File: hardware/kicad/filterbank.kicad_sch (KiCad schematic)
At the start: 76 parts, among them J3 SMA/EDGE(RTL-SDR), U11 PE42582A(QFN24), U8 PE42582A(QFN24)

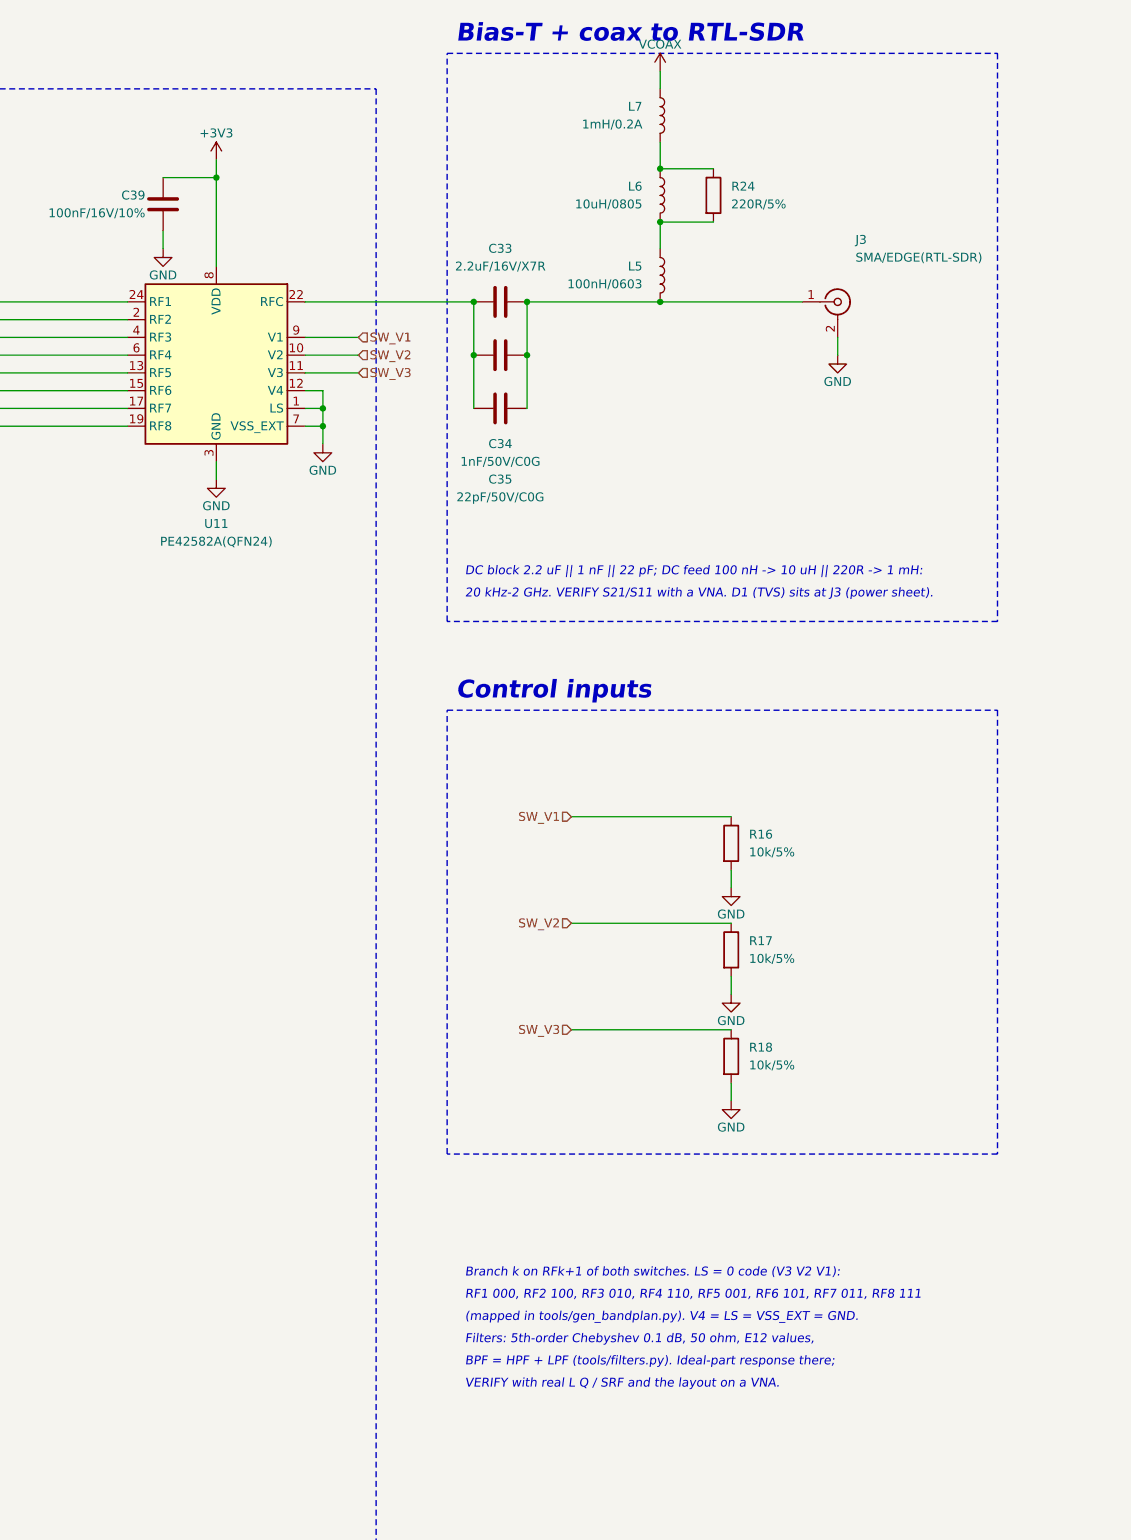
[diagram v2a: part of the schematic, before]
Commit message: U11 with LS = 1: mirror-port pairing makes the filter bank planar
PE42582 truth table: LS = 1 selects port 9 - port(LS = 0) for the same
V code, so U8 RF(k+1) pairs with U11 RF(8-k) and the 8 branches run
between the two facing switches on F.Cu without crossings. Same V lines,
firmware unchanged; at reset (V = 000) U8 RF1 / U11 RF8 = F0 THRU.
Symbol variant PE42582R (ports listed RF8..RF1, LS on top).

Co-Authored-By: Claude Opus 5.5 <noreply@anthropic.com>
Claude-Session: https://claude.ai/code/session_01YRUiF8Vp4242sya9Xyg3TV
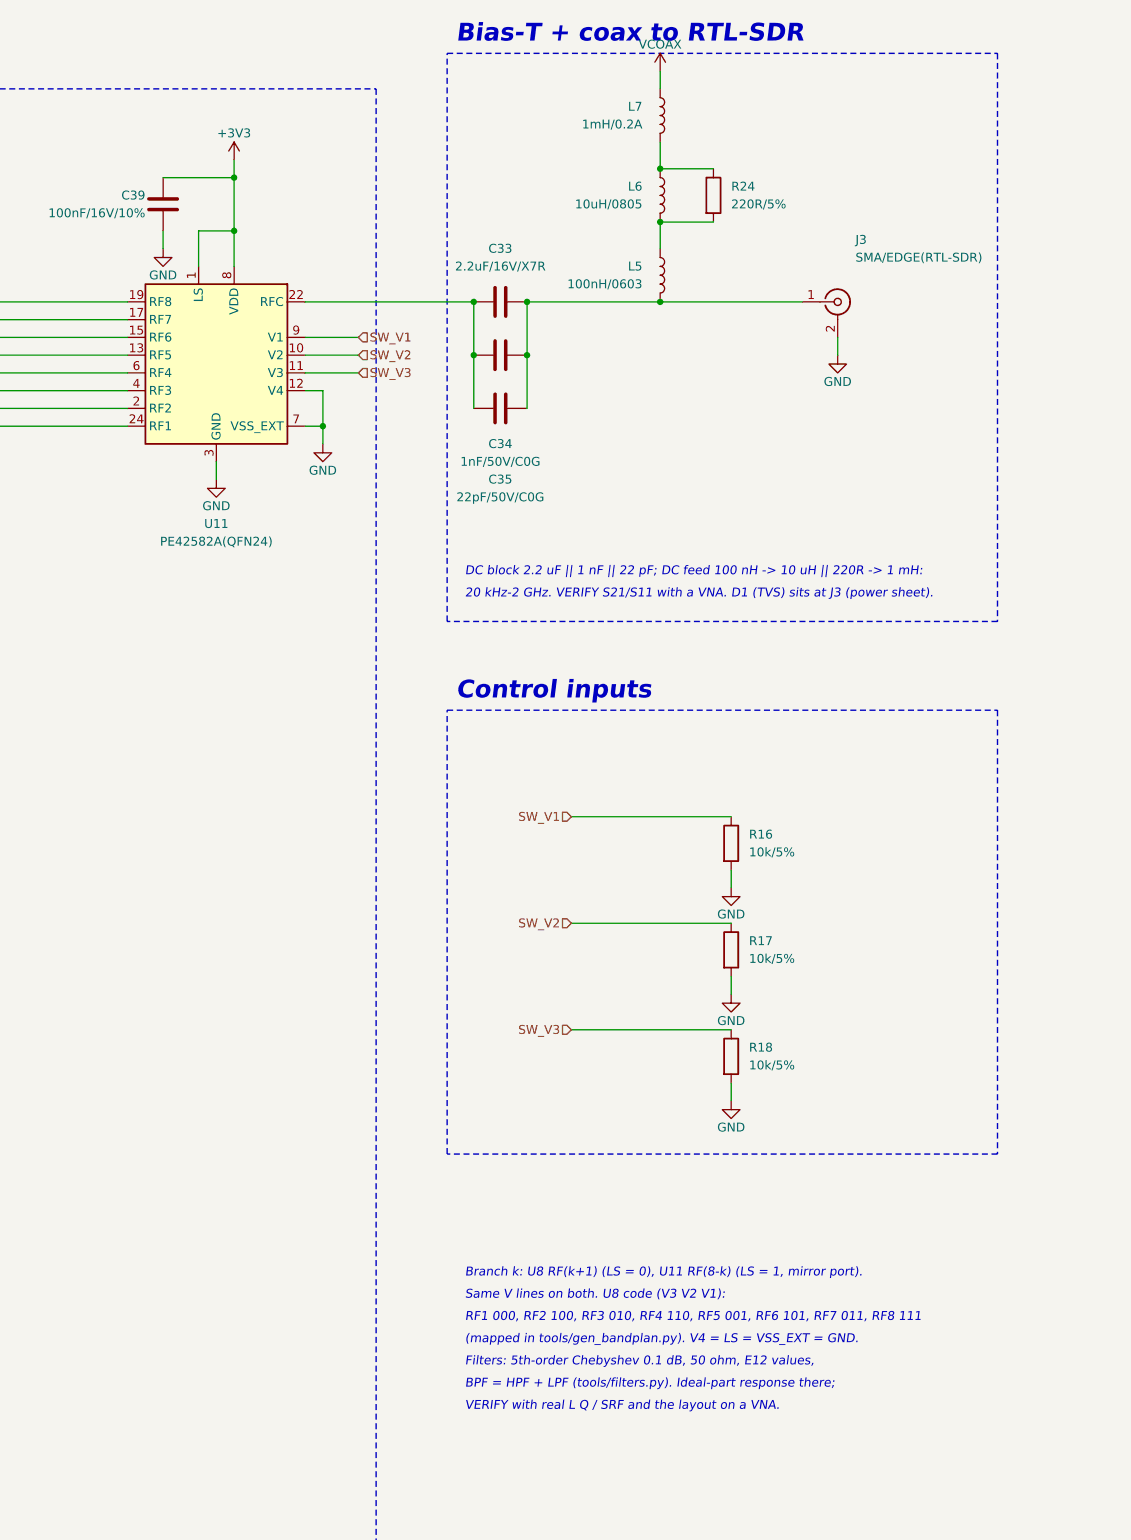
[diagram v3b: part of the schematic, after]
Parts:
- removed U11: PE42582A(QFN24), Package_DFN_QFN:QFN-24-1EP_4x4mm_P0.5mm_EP2.6x2.6mm, symbol coaxolotl:PE42582
- added U11: PE42582A(QFN24), Package_DFN_QFN:QFN-24-1EP_4x4mm_P0.5mm_EP2.6x2.6mm, symbol coaxolotl:PE42582R
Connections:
- net +3V3: now also U11.1 (LS), U11.8 (VDD)
- net GND: now also U11.12 (V4), U11.14 (GND), U11.16 (GND), U11.18 (GND), U11.20 (GND), U11.21 (GND), U11.23 (GND), U11.25 (GND), U11.3 (GND), U11.5 (GND), U11.7 (VSS_EXT)
- net SW_V1: now also U11.9 (V1)
- net SW_V2: now also U11.10 (V2)
- net SW_V3: now also U11.11 (V3)
- net at C406.1, L404.2: now also U11.6 (RF4)
- net at C103.1, L102.2: now also U11.17 (RF7)
- net at C33.1, C34.1, C35.1: now also U11.22 (RFC)
- net at C606.1, L604.2: now also U11.2 (RF2)
- net at C506.1, L504.2: now also U11.4 (RF3)
- net at C206.1, L204.2: now also U11.15 (RF6)
- net at C703.2: now also U11.24 (RF1)
- net at R21.2: now also U11.19 (RF8)
- net at C306.1, L304.2: now also U11.13 (RF5)
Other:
- note added: "Branch k: U8 RF(k+1) (LS = 0), U11 RF(8-k) (LS = 1, mirror port)."
- note added: "Same V lines on both. U8 code (V3 V2 V1):"
- note removed: "Branch k on RFk+1 of both switches. LS = 0 code (V3 V2 V1):"

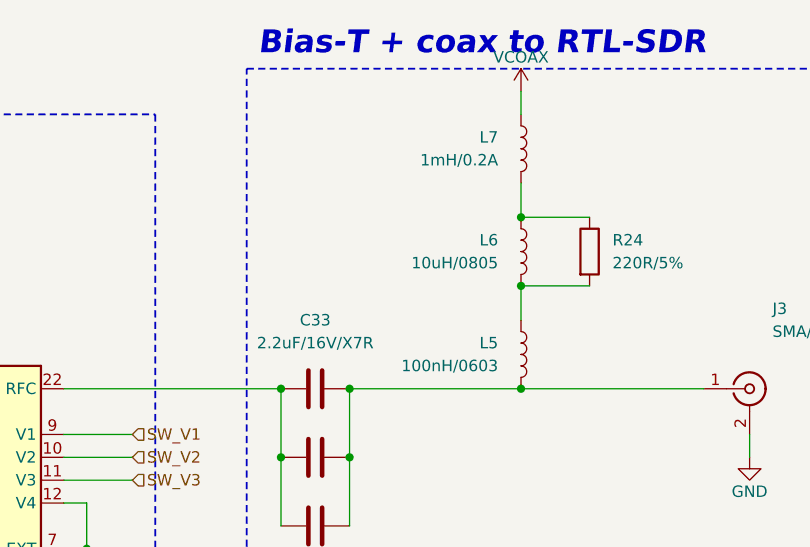
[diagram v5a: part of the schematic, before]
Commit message: L6: 10 uH 1210 wire-wound, 450 mA (LQH32CN100K33L, C86069) - it carries the whole coax DC
Co-Authored-By: Claude Opus 5.5 <noreply@anthropic.com>
Claude-Session: https://claude.ai/code/session_01YRUiF8Vp4242sya9Xyg3TV
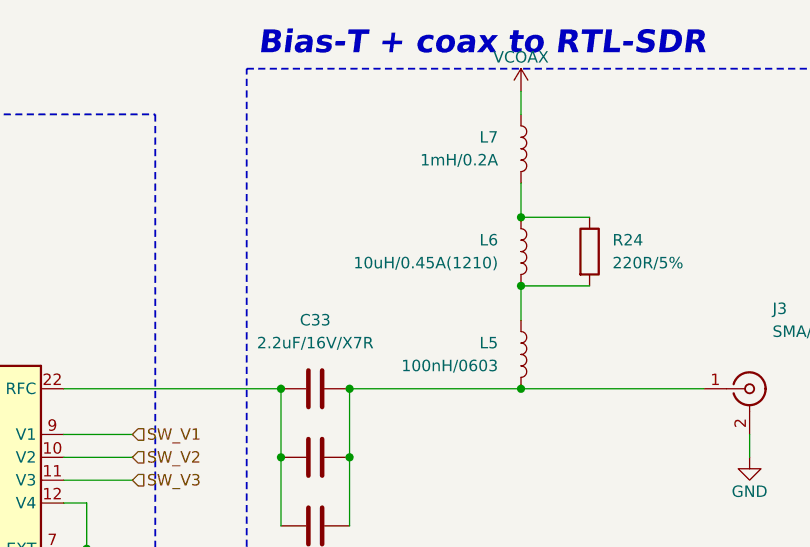
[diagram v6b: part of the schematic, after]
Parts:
- L6: value 10uH/0805 -> 10uH/0.45A(1210); footprint Inductor_SMD:L_0805_2012Metric -> Inductor_SMD:L_1210_3225Metric; MPN (none) -> LQH32CN100K33L

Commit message: Filter bank F7 retuned for the pad capacitance; LCSC codes for every fitted part; C10/J1/TP1/TP6 DNP
F7 (70/23cm HPF): C701/C703 12 pF, C702 6.8 pF, L701/L702 10 nH (was 8.2p/4.7p/15n), from the
openEMS lane N-port co-simulation (simu/f7_retune.py). filters.LAYOUT_TUNED carries the values.
L403/L404: Murata LQW18ANR33G00D C162651 (ceramic core) replaces LQW18CAR33J00D.
New codes, checked on JLC/LCSC (EasyEDA API) 2026-10-28: 12pF C38523, 6.8pF C1679, 10nH C15666,
820pF C701305, 1.5uH C317997, 2.2uH C41651, 4.7uH C139136.
Schematic sheets patched in place (build.py writes random uuids; the routed board links to the
current ones); build.py carries the same changes.

Co-Authored-By: Claude Opus 5.5 <noreply@anthropic.com>
Claude-Session: https://claude.ai/code/session_01YRUiF8Vp4242sya9Xyg3TV
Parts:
- C701, C703: value 8.2pF/50V/C0G -> 12pF/50V/C0G
- C702: value 4.7pF/50V/C0G -> 6.8pF/50V/C0G
- L701, L702: value 15nH/5% -> 10nH/5%
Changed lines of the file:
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@@
       )
     )
-    (property "Value" "8.2pF/50V/C0G"
+    (property "Value" "12pF/50V/C0G"
       (at 83.82 234.95 90)
       (effects
@@
       )
     )
-    (property "Value" "15nH/5%"
+    (property "Value" "10nH/5%"
       (at 101.6 245.11 0)
       (effects
@@
       )
     )
-    (property "Value" "4.7pF/50V/C0G"
+    (property "Value" "6.8pF/50V/C0G"
       (at 114.3 234.95 90)
       (effects
@@
       )
     )
-    (property "Value" "15nH/5%"
+    (property "Value" "10nH/5%"
       (at 132.08 245.11 0)
       (effects
@@
       )
     )
-    (property "Value" "8.2pF/50V/C0G"
+    (property "Value" "12pF/50V/C0G"
       (at 144.78 234.95 90)
       (effects

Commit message: MCU to EFM8BB21F16G-C-QFN20 (QSOP24 end of life), BWSMA-KE-P001 edge SMA, Brightking GDT
U5: QFN20, all 16 port pins used. TP_TX test point dropped; LED_OE_N on P0.4, lamp chain on
P1.4-P1.6, LNA_PATH_OUT on P1.3, FMN on P2.0/C2D through R30 1k (debugger overrides it).
Footprint from the LCSC C80713 land pattern. Firmware HAL and docs/hardware.md follow;
179/179 host tests pass, SDCC build OK.
J2/J3: BAT WIRELESS BWSMA-KE-P001 (C496550) edge launch, footprint from LCSC, board edge at
local x = +2.70 mm. GDT1: Brightking 4532-091-LF (C78323), same 1812 land pattern.
check.py: netlist matches the intent.

Co-Authored-By: Claude Opus 5.5 <noreply@anthropic.com>
Claude-Session: https://claude.ai/code/session_01YRUiF8Vp4242sya9Xyg3TV
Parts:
- J3: footprint Connector_Coaxial:SMA_Amphenol_132289_EdgeMount -> coaxolotl:SMA_EdgeLaunch_BWSMA-KE-P001
